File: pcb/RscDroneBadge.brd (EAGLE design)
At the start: 160 x 100 mm, 31 parts, among them Q1 BC547, Q2 BC547, Q3 BC547, Q4 BC547

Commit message: update schematic and board, add drawing
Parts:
- added BAT: CR2032_PLASTIC, BASTL_BATHOLDER:CR2032_PLASTIC
- R1, R2, R3, R4, R5, R6, R7, R8: device BASTL_RESISTORS:RCL_0204/7_ROUND -> BASTL_RESISTORS:RCL_0207
- moved R8 94.7 mm to (22.0, -14.0), turned to 315 degrees
- moved R4 92.0 mm to (14.0, -22.0), turned to 315 degrees
- moved LD12 90.3 mm to (28.0, -33.6), turned to 270 degrees
- moved LD8 88.0 mm to (28.0, -22.4), turned to 90 degrees
- moved LD16 87.9 mm to (33.6, -28.0)
- moved Q4 87.6 mm to (18.0, -18.0), turned to 225 degrees
- moved C1 74.4 mm to (18.5, 7.00)
- moved R6 72.9 mm to (-14.0, -22.0), turned to 225 degrees
- moved LD7 70.9 mm to (28.0, 33.6), turned to 90 degrees
- moved R3 68.0 mm to (22.0, 14.0), turned to 45 degrees
- moved LD4 67.1 mm to (22.4, -28.0), turned to 180 degrees
- moved LD10 64.3 mm to (-28.0, -33.6), turned to 270 degrees
- moved LD14 64.0 mm to (-22.4, -28.0)
- moved Q3 63.6 mm to (18.0, 18.0), turned to 315 degrees
- moved R2 60.0 mm to (-22.0, -14.0), turned to 225 degrees
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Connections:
- net GND: now also BAT.N
- net VDD: now also BAT.P
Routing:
- net GND: track 0.00 -> 31.2 mm
- added copper zone on layer 1, net GND
- added copper zone on layer 1, net GND1
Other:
- board size 160 x 100 mm -> 77 x 77 mm
- board text added: "MODE ON/OFF"
- board text added: "Resistance Support Collective 2024"

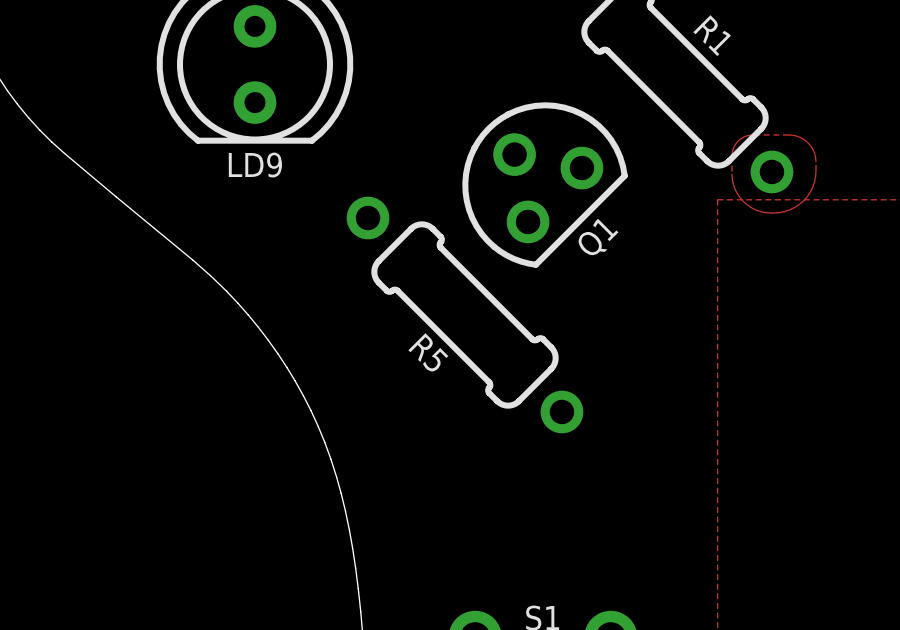
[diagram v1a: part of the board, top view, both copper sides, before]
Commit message: alignment fix
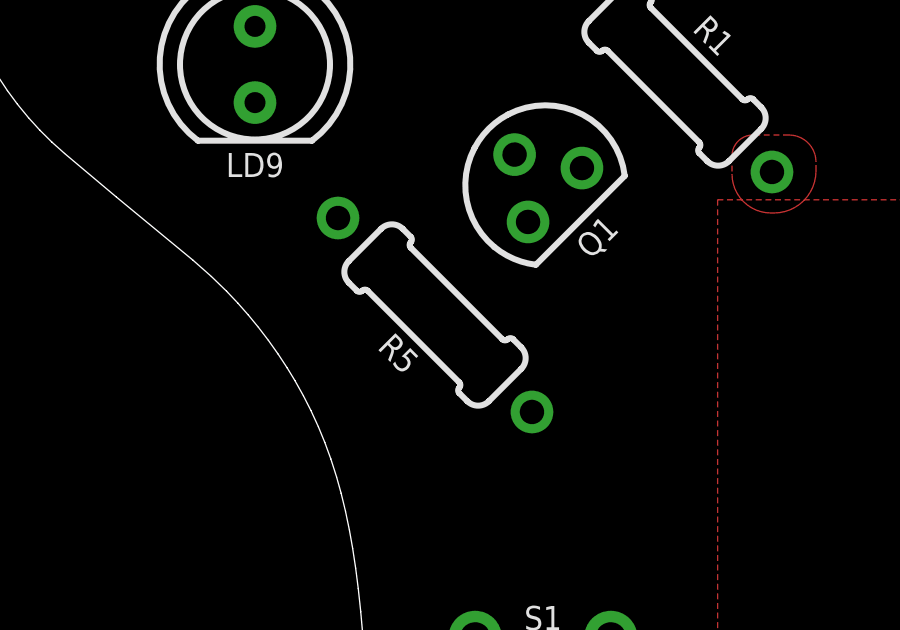
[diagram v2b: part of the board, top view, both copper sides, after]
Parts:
- moved R5 1.00 mm to (-22.0, 14.0)
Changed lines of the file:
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@@
 <grid distance="1" unitdist="mm" unit="mm" style="lines" multiple="1" display="yes" altdistance="0.01" altunitdist="mm" altunit="mm"/>
 <layers>
-<layer number="1" name="Top" color="4" fill="1" visible="no" active="yes"/>
+<layer number="1" name="Top" color="4" fill="1" visible="yes" active="yes"/>
 <layer number="2" name="Route2" color="16" fill="1" visible="no" active="no"/>
 <layer number="3" name="Route3" color="17" fill="1" visible="no" active="no"/>
@@
 <layer number="14" name="Route14" color="22" fill="1" visible="no" active="no"/>
 <layer number="15" name="Route15" color="23" fill="1" visible="no" active="no"/>
-<layer number="16" name="Bottom" color="1" fill="1" visible="no" active="yes"/>
-<layer number="17" name="Pads" color="2" fill="1" visible="no" active="yes"/>
-<layer number="18" name="Vias" color="2" fill="1" visible="no" active="yes"/>
-<layer number="19" name="Unrouted" color="6" fill="1" visible="no" active="yes"/>
-<layer number="20" name="Dimension" color="24" fill="1" visible="no" active="yes"/>
-<layer number="21" name="tPlace" color="7" fill="1" visible="no" active="yes"/>
-<layer number="22" name="bPlace" color="7" fill="1" visible="no" active="yes"/>
-<layer number="23" name="tOrigins" color="15" fill="1" visible="no" active="yes"/>
-<layer number="24" name="bOrigins" color="15" fill="1" visible="no" active="yes"/>
+<layer number="16" name="Bottom" color="1" fill="1" visible="yes" active="yes"/>
+<layer number="17" name="Pads" color="2" fill="1" visible="yes" active="yes"/>
+<layer number="18" name="Vias" color="2" fill="1" visible="yes" active="yes"/>
+<layer number="19" name="Unrouted" color="6" fill="1" visible="yes" active="yes"/>
+<layer number="20" name="Dimension" color="24" fill="1" visible="yes" active="yes"/>
+<layer number="21" name="tPlace" color="7" fill="1" visible="yes" active="yes"/>
+<layer number="22" name="bPlace" color="7" fill="1" visible="yes" active="yes"/>
+<layer number="23" name="tOrigins" color="15" fill="1" visible="yes" active="yes"/>
+<layer number="24" name="bOrigins" color="15" fill="1" visible="yes" active="yes"/>
 <layer number="25" name="tNames" color="7" fill="1" visible="yes" active="yes"/>
-<layer number="26" name="bNames" color="7" fill="1" visible="no" active="yes"/>
+<layer number="26" name="bNames" color="7" fill="1" visible="yes" active="yes"/>
 <layer number="27" name="tValues" color="7" fill="1" visible="no" active="yes"/>
 <layer number="28" name="bValues" color="7" fill="1" visible="no" active="yes"/>
@@
 <layer number="37" name="tTest" color="7" fill="1" visible="no" active="yes"/>
 <layer number="38" name="bTest" color="7" fill="1" visible="no" active="yes"/>
-<layer number="39" name="tKeepout" color="4" fill="11" visible="no" active="yes"/>
-<layer number="40" name="bKeepout" color="1" fill="11" visible="no" active="yes"/>
-<layer number="41" name="tRestrict" color="4" fill="10" visible="no" active="yes"/>
-<layer number="42" name="bRestrict" color="1" fill="10" visible="no" active="yes"/>
+<layer number="39" name="tKeepout" color="4" fill="11" visible="yes" active="yes"/>
+<layer number="40" name="bKeepout" color="1" fill="11" visible="yes" active="yes"/>
+<layer number="41" name="tRestrict" color="4" fill="10" visible="yes" active="yes"/>
+<layer number="42" name="bRestrict" color="1" fill="10" visible="yes" active="yes"/>
 <layer number="43" name="vRestrict" color="2" fill="10" visible="no" active="yes"/>
 <layer number="44" name="Drills" color="7" fill="1" visible="no" active="yes"/>
@@
 <layer number="49" name="Reference" color="7" fill="1" visible="no" active="yes"/>
 <layer number="50" name="dxf" color="7" fill="1" visible="no" active="no"/>
-<layer number="51" name="tDocu" color="7" fill="1" visible="no" active="yes"/>
-<layer number="52" name="bDocu" color="7" fill="1" visible="no" active="yes"/>
+<layer number="51" name="tDocu" color="7" fill="1" visible="yes" active="yes"/>
+<layer number="52" name="bDocu" color="7" fill="1" visible="yes" active="yes"/>
 <layer number="53" name="tGND_GNDA" color="7" fill="1" visible="no" active="no"/>
 <layer number="54" name="bGND_GNDA" color="7" fill="1" visible="no" active="no"/>
@@
 </layers>
 <board>
-<fusionsync huburn="a.YnVzaW5lc3M6YmFzdGxpbnN0cnVtZW50cw" projecturn="a.YnVzaW5lc3M6YmFzdGxpbnN0cnVtZW50cyNEMjAyMjAzMTQ1MDY5Nzg3MDE" f3durn="urn:adsk.wipprod:dm.lineage:hj-RkZzyTciGFN7Iz4JQvQ" pcbguid="" lastpulledtime="" lastsyncedchangeguid="" latestrevisionid="66975d14-4276-45ca-8036-a6ac9c8b5085" lastsyncedrevisionid="66975d14-4276-45ca-8036-a6ac9c8b5085" lastboardhashguid="f90bc22c-0f56-8191-0fa9-85b619ea2516" lastpushedtime="2024-03-29T21:06:01Z" linktopcb3d="true"/>
+<fusionsync huburn="a.YnVzaW5lc3M6YmFzdGxpbnN0cnVtZW50cw" projecturn="a.YnVzaW5lc3M6YmFzdGxpbnN0cnVtZW50cyNEMjAyMjAzMTQ1MDY5Nzg3MDE" f3durn="urn:adsk.wipprod:dm.lineage:hj-RkZzyTciGFN7Iz4JQvQ" pcbguid="" lastpulledtime="" lastsyncedchangeguid="" latestrevisionid="66975d14-4276-45ca-8036-a6ac9c8b5085" lastsyncedrevisionid="66975d14-4276-45ca-8036-a6ac9c8b5085" lastboardhashguid="f90bc22c-0f56-8191-0fa9-85b619ea2516" lastpushedtime="2024-03-29T21:06:01Z" linktopcb3d="false"/>
 <plain>
 <wire x1="-18.843065625" y1="34.889540625" x2="-19.219071875" y2="35.31045625" width="0.001" layer="20"/>
@@
 <attribute name="VALUE" x="14" y="-22" size="0.8" layer="27" ratio="15" rot="R315" align="center"/>
 </element>
-<element name="R5" library="BASTL_RESISTORS" library_urn="urn:adsk.eagle:library:32975925" package="RCL_0207" package3d_urn="urn:adsk.eagle:package:43822012/4" value="10" x="-21" y="14" smashed="yes" rot="R135">
-<attribute name="NAME" x="-22.2057875" y="12.71460625" size="0.8" layer="25" ratio="15" rot="R135" align="center"/>
-<attribute name="VALUE" x="-21" y="14" size="0.8" layer="27" ratio="15" rot="R135" align="center"/>
+<element name="R5" library="BASTL_RESISTORS" library_urn="urn:adsk.eagle:library:32975925" package="RCL_0207" package3d_urn="urn:adsk.eagle:package:43822012/4" value="10" x="-22" y="14" smashed="yes" rot="R135">
+<attribute name="NAME" x="-23.2057875" y="12.71460625" size="0.8" layer="25" ratio="15" rot="R135" align="center"/>
+<attribute name="VALUE" x="-22" y="14" size="0.8" layer="27" ratio="15" rot="R135" align="center"/>
 </element>
 <element name="R6" library="BASTL_RESISTORS" library_urn="urn:adsk.eagle:library:32975925" package="RCL_0207" package3d_urn="urn:adsk.eagle:package:43822012/4" value="10" x="-14" y="-22" smashed="yes" rot="R225">
@@
 <contactref element="Q1" pad="3"/>
 <contactref element="R5" pad="1"/>
-<wire x1="-18.898025" y1="17.101971875" x2="-17.76710625" y2="10.76710625" width="0" layer="19" extent="1-1"/>
+<wire x1="-18.898025" y1="17.101971875" x2="-18.76710625" y2="10.76710625" width="0" layer="19" extent="1-1"/>
 </signal>
 <signal name="N$11">
@@
 <contactref element="LD2" pad="K"/>
 <contactref element="LD3" pad="K"/>
-<wire x1="-24.232890625" y1="17.232890625" x2="-34.92" y2="-28" width="0" layer="19" extent="1-1"/>
-<wire x1="-34.92" y1="28" x2="-24.232890625" y2="17.232890625" width="0" layer="19" extent="1-1"/>
-<wire x1="21.08" y1="28" x2="-24.232890625" y2="17.232890625" width="0" layer="19" extent="1-1"/>
+<wire x1="-25.232890625" y1="17.232890625" x2="-34.92" y2="-28" width="0" layer="19" extent="1-1"/>
+<wire x1="-34.92" y1="28" x2="-25.232890625" y2="17.232890625" width="0" layer="19" extent="1-1"/>
+<wire x1="21.08" y1="28" x2="-25.232890625" y2="17.232890625" width="0" layer="19" extent="1-1"/>
 <wire x1="21.08" y1="-28" x2="-34.92" y2="-28" width="0" layer="19" extent="1-1"/>
 </signal>

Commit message: routing
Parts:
- added ISP: 2X3POGONO_VIA, BASTL_CONNECTORS:2X3_POGO_NO_VIA
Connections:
- removed net N$5: IC1.5, R1.1
- removed net N$6: IC1.6, R2.1
- removed net N$7: IC1.7, R3.1
- new net MISO: IC1.6, ISP.P$1, R2.1
- new net MOSI: IC1.5, ISP.P$4, R1.1
- new net RST: IC1.1, ISP.P$5
- new net SCK: IC1.7, ISP.P$3, R3.1
- net GND: now also ISP.P$6
- net VDD: now also ISP.P$2
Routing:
- net VDD: track 0.00 -> 288.6 mm, vias 0 -> 1
- net N$20: track 0.00 -> 212.7 mm
- net N$14: track 0.00 -> 208.5 mm
- net N$15: track 0.00 -> 208.2 mm
- net N$19: track 0.00 -> 197.5 mm
- net MOSI: track 0.00 -> 93.5 mm, vias 0 -> 2
- net GND: track 31.2 -> 121.4 mm, vias 0 -> 2
- net MISO: track 0.00 -> 83.0 mm, vias 0 -> 1
- net N$1: track 0.00 -> 55.3 mm
- net SCK: track 0.00 -> 29.6 mm, vias 0 -> 1
- net N$9: track 0.00 -> 25.6 mm
- net RST: track 0.00 -> 6.88 mm
- net N$8: track 0.00 -> 6.76 mm
- net N$4: track 0.00 -> 6.76 mm
- net N$3: track 0.00 -> 6.76 mm
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
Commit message: finishing
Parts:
- BAT: value CR2032_PLASTIC -> CR2032 HOLDER
- IC1: value (none) -> ATTINY85
- S1: value PUSH_MOMENTARY_THT_6X6MM -> 6x6mm BUTTON
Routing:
- net MOSI: track 93.5 -> 100.5 mm
- net N$20: track 212.7 -> 207.0 mm
- net N$19: track 197.5 -> 202.8 mm, vias 0 -> 1
- net N$9: track 25.6 -> 22.2 mm
- net N$15: track 208.2 -> 211.4 mm, vias 0 -> 1
- net VDD: track 288.6 -> 285.4 mm
- net N$14: track 208.5 -> 210.9 mm
- net GND: track 121.4 -> 123.7 mm
- net N$11: track 6.39 -> 8.63 mm
- net MISO: track 83.0 -> 84.7 mm
- net SCK: track 29.6 -> 31.1 mm
- net N$12: track 6.39 -> 7.71 mm
- net N$1: track 55.3 -> 56.5 mm
- removed copper zone on layer 1, net GND
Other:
- board text added: "3.3V"
- board text added: "RESISTANCE SUPPORT CLUB 2024"
- board text removed: "Resistance Support Collective 2024"

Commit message: remove "85" from ATTINY label on the board
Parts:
- IC1: value ATTINY85 -> ATTINY
